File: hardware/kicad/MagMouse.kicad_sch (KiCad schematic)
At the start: 0 parts

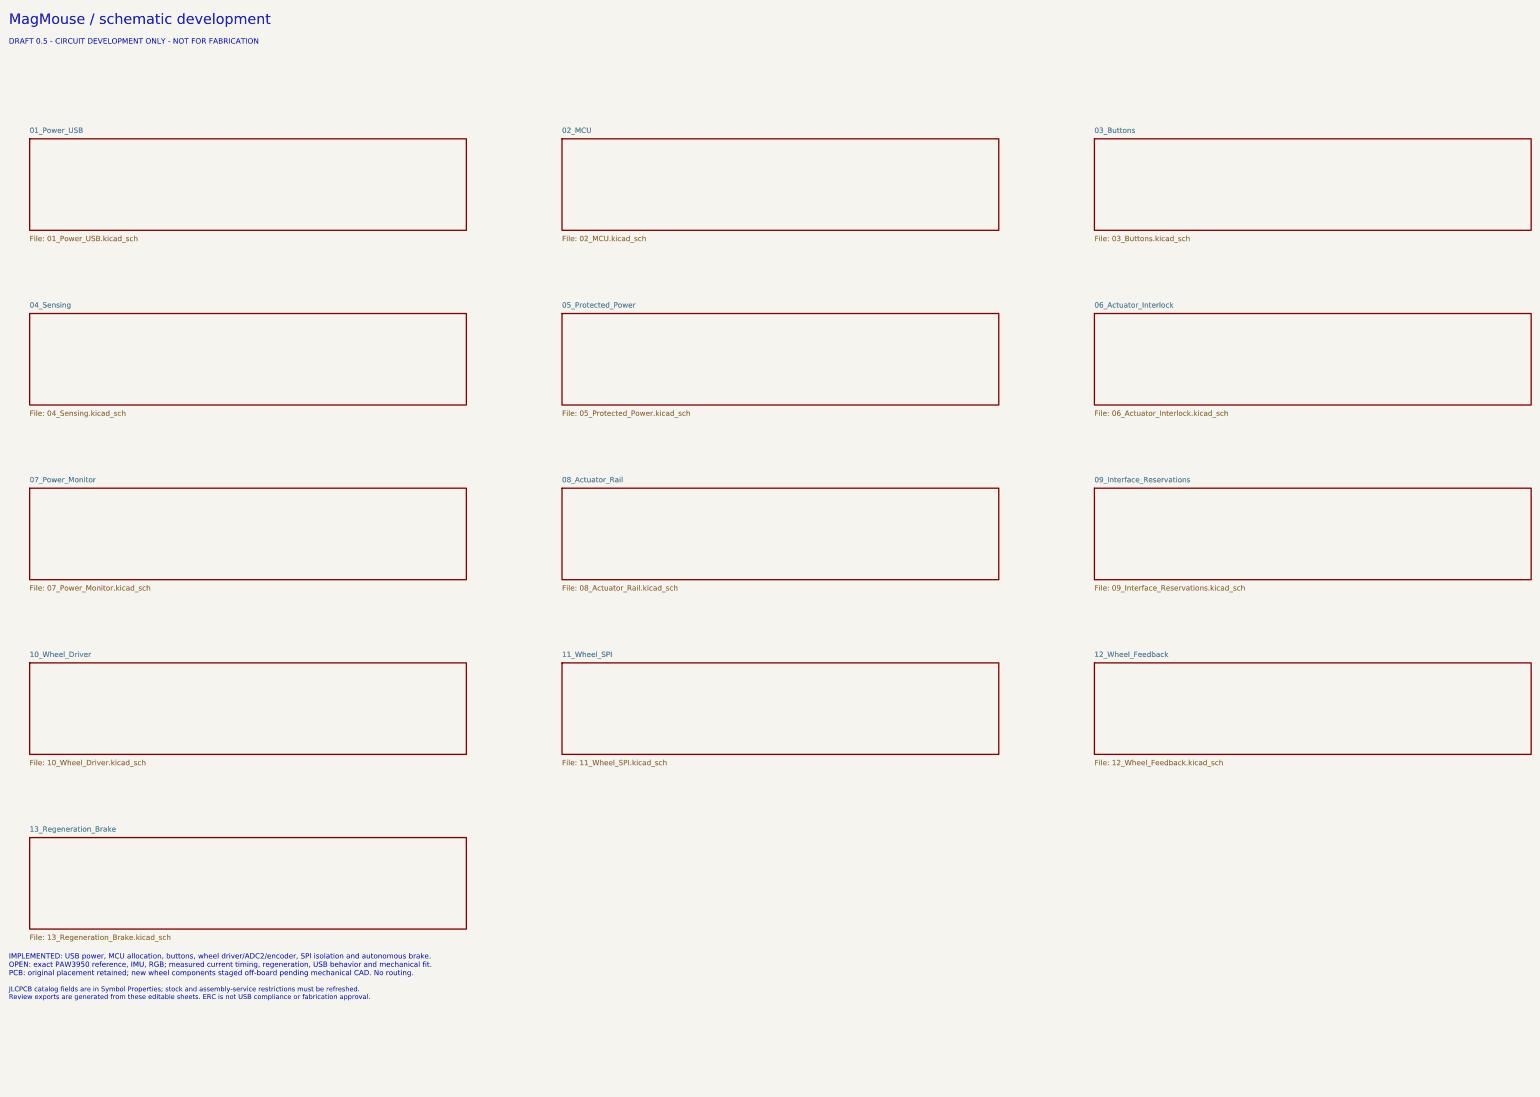
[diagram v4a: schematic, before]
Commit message: Add IMU and RGB circuits and document optical sourcing
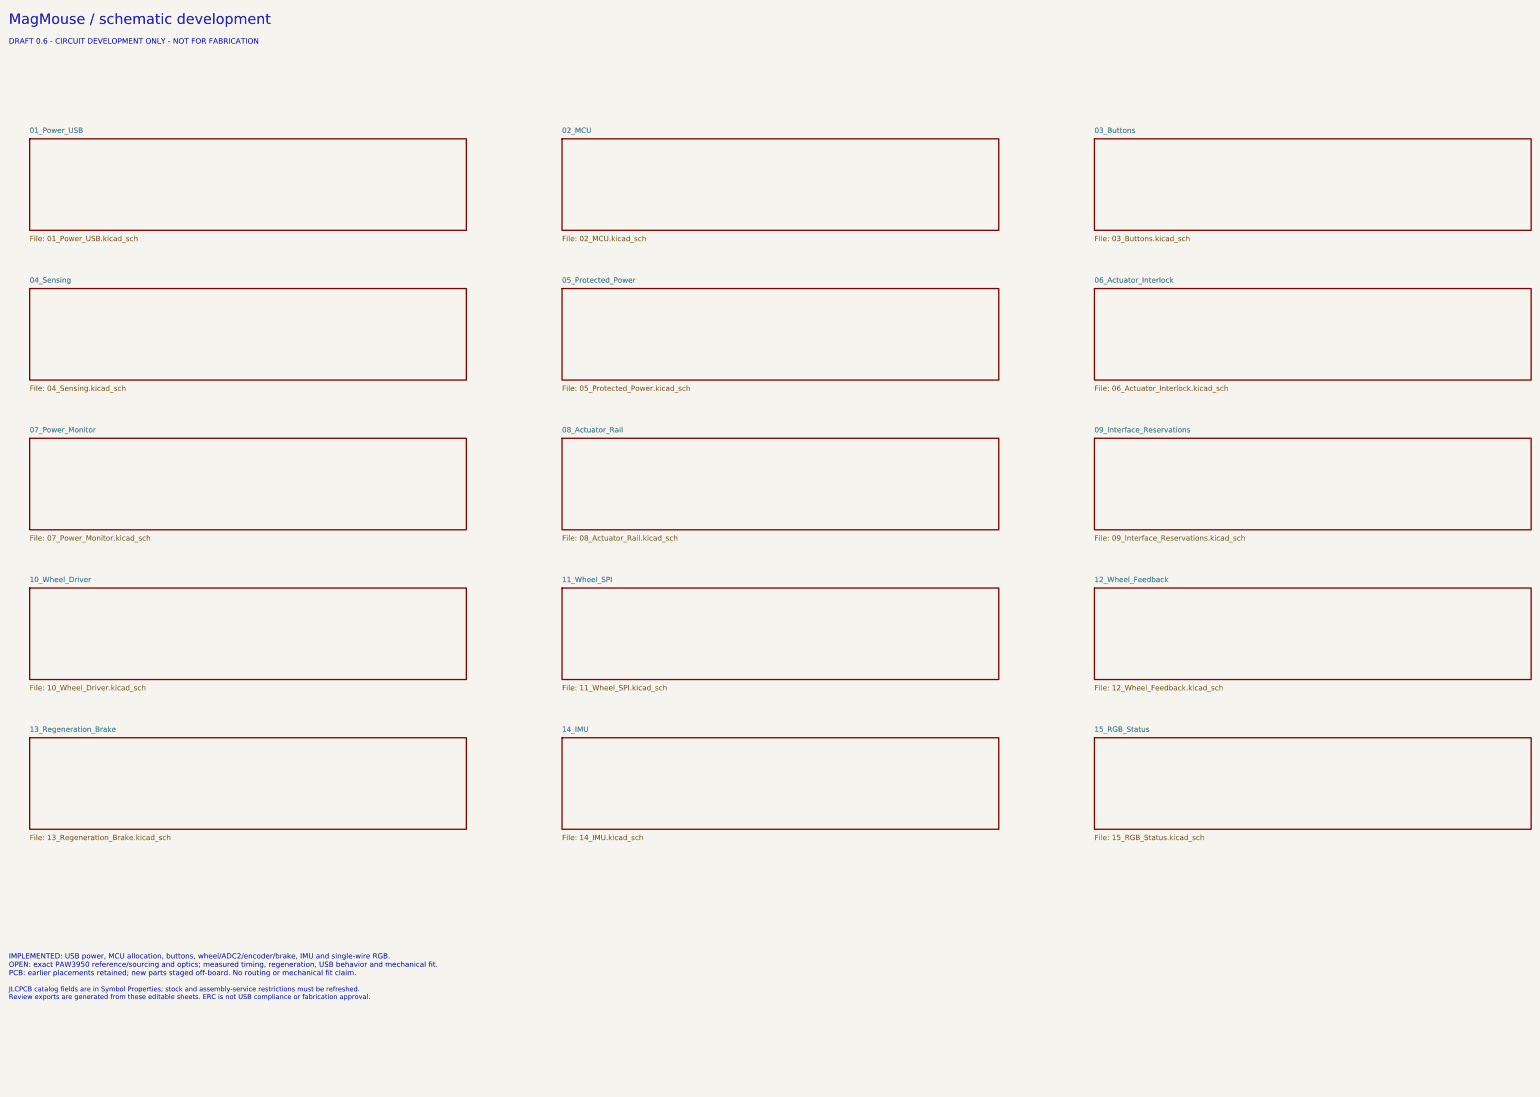
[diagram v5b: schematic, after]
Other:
- added sheet 14_IMU (14_IMU.kicad_sch)
- added sheet 15_RGB_Status (15_RGB_Status.kicad_sch)
- note added: "DRAFT 0.6 - CIRCUIT DEVELOPMENT ONLY - NOT FOR FABRICATION"
- note added: "IMPLEMENTED: USB power, MCU allocation, buttons, wheel/ADC2/encoder/brake, IMU and single-wire RGB. OPEN: exact PAW3950 reference/sourcing and optics; measured timing, regeneration, USB behavior and mechanical fit. PCB: earlier placements retained; new parts staged off-board. No routing or mechanical fit claim."
- note removed: "DRAFT 0.5 - CIRCUIT DEVELOPMENT ONLY - NOT FOR FABRICATION"
- note removed: "IMPLEMENTED: USB power, MCU allocation, buttons, wheel driver/ADC2/encoder, SPI isolation and autonomous brake. OPEN: exact PAW3950 reference, IMU, RGB; measured current timing, regeneration, USB behavior and mechanical fit. PCB: original placement retained; new wheel components staged off-board pending mechanical CAD. No routing."
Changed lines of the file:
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@@
     (title "MagMouse - MagMouse")
     (date "2026-09-09")
-    (rev "0.5 DRAFT")
+    (rev "0.6 DRAFT")
     (company "MagMouse")
     (comment 1 "NOT FOR FABRICATION - unresolved circuits listed in README.md"))
@@
       (justify left top))
 )
-  (text "DRAFT 0.5 - CIRCUIT DEVELOPMENT ONLY - NOT FOR FABRICATION"
+  (text "DRAFT 0.6 - CIRCUIT DEVELOPMENT ONLY - NOT FOR FABRICATION"
     (at 20 24 0)
     (effects
@@
           (page "4")))))
   (sheet
-    (at 25 90)
+    (at 25 84)
     (size 105 22)
     (stroke
@@
       (color 0 0 0 0))
     (property "Sheetname" "04_Sensing"
-      (at 25 88.73 0)
+      (at 25 82.73 0)
       (effects
         (font
@@
         (justify left bottom)))
     (property "Sheetfile" "04_Sensing.kicad_sch"
-      (at 25 113.27 0)
+      (at 25 107.27 0)
       (effects
         (font
@@
           (page "5")))))
   (sheet
-    (at 153 90)
+    (at 153 84)
     (size 105 22)
     (stroke
@@
       (color 0 0 0 0))
     (property "Sheetname" "05_Protected_Power"
-      (at 153 88.73 0)
+      (at 153 82.73 0)
       (effects
         (font
@@
         (justify left bottom)))
     (property "Sheetfile" "05_Protected_Power.kicad_sch"
-      (at 153 113.27 0)
+      (at 153 107.27 0)
       (effects
         (font
@@
           (page "6")))))
   (sheet
-    (at 281 90)
+    (at 281 84)
     (size 105 22)
     (stroke
@@
       (color 0 0 0 0))
     (property "Sheetname" "06_Actuator_Interlock"
-      (at 281 88.73 0)
+      (at 281 82.73 0)
       (effects
         (font
@@
         (justify left bottom)))
     (property "Sheetfile" "06_Actuator_Interlock.kicad_sch"
-      (at 281 113.27 0)
+      (at 281 107.27 0)
       (effects
         (font
@@
           (page "7")))))
   (sheet
-    (at 25 132)
+    (at 25 120)
     (size 105 22)
     (stroke
@@
       (color 0 0 0 0))
     (property "Sheetname" "07_Power_Monitor"
-      (at 25 130.73 0)
+      (at 25 118.73 0)
       (effects
         (font
@@
         (justify left bottom)))
     (property "Sheetfile" "07_Power_Monitor.kicad_sch"
-      (at 25 155.27 0)
+      (at 25 143.27 0)
       (effects
         (font
@@
           (page "8")))))
   (sheet
-    (at 153 132)
+    (at 153 120)
     (size 105 22)
     (stroke
@@
       (color 0 0 0 0))
     (property "Sheetname" "08_Actuator_Rail"
-      (at 153 130.73 0)
+      (at 153 118.73 0)
       (effects
         (font
@@
         (justify left bottom)))
     (property "Sheetfile" "08_Actuator_Rail.kicad_sch"
-      (at 153 155.27 0)
+      (at 153 143.27 0)
       (effects
         (font
@@
         (path "/5d73110b-42e6-5c5c-9841-c82d60f67640"
           (page "9")))))
-  (text "IMPLEMENTED: USB power, MCU allocation, buttons, wheel driver/ADC2/encoder, SPI isolation and autonomous brake.\nOPEN: exact PAW3950 reference, IMU, RGB; measured current timing, regeneration, USB behavior and mechanical fit.\nPCB: original placement retained; new wheel components staged off-board pending mechanical CAD. No routing."
+  (text "IMPLEMENTED: USB power, MCU allocation, buttons, wheel/ADC2/encoder/brake, IMU and single-wire RGB.\nOPEN: exact PAW3950 reference/sourcing and optics; measured timing, regeneration, USB behavior and mechanical fit.\nPCB: earlier placements retained; new parts staged off-board. No routing or mechanical fit claim."
     (at 20 244 0)
     (effects
@@
   (embedded_fonts no)
   (sheet
-    (at 281 132)
+    (at 281 120)
     (size 105 22)
     (stroke
@@
       (color 0 0 0 0))
     (property "Sheetname" "09_Interface_Reservations"
-      (at 281 130.73 0)
+      (at 281 118.73 0)
       (effects
         (font
@@
         (justify left bottom)))
     (property "Sheetfile" "09_Interface_Reservations.kicad_sch"
-      (at 281 155.27 0)
+      (at 281 143.27 0)
       (effects
         (font
@@
           (page "10")))))
   (sheet
-    (at 25 174)
+    (at 25 156)
     (size 105 22)
     (stroke
@@
       (color 0 0 0 0))
     (property "Sheetname" "10_Wheel_Driver"
-      (at 25 172.73 0)
+      (at 25 154.73 0)
       (effects
         (font
@@
         (justify left bottom)))
     (property "Sheetfile" "10_Wheel_Driver.kicad_sch"
-      (at 25 197.27 0)
+      (at 25 179.27 0)
       (effects
         (font
@@
           (page "11")))))
   (sheet
-    (at 153 174)
+    (at 153 156)
     (size 105 22)
     (stroke
@@
       (color 0 0 0 0))
     (property "Sheetname" "11_Wheel_SPI"
-      (at 153 172.73 0)
+      (at 153 154.73 0)
       (effects
         (font
@@
         (justify left bottom)))
     (property "Sheetfile" "11_Wheel_SPI.kicad_sch"
-      (at 153 197.27 0)
+      (at 153 179.27 0)
       (effects
         (font
@@
           (page "12")))))
   (sheet
-    (at 281 174)
+    (at 281 156)
     (size 105 22)
     (stroke
@@
       (color 0 0 0 0))
     (property "Sheetname" "12_Wheel_Feedback"
-      (at 281 172.73 0)
+      (at 281 154.73 0)
       (effects
         (font
@@
         (justify left bottom)))
     (property "Sheetfile" "12_Wheel_Feedback.kicad_sch"
-      (at 281 197.27 0)
+      (at 281 179.27 0)
       (effects
         (font
@@
           (page "13")))))
   (sheet
-    (at 25 216)
+    (at 25 192)
     (size 105 22)
     (stroke
@@
       (color 0 0 0 0))
     (property "Sheetname" "13_Regeneration_Brake"
-      (at 25 214.73 0)
+      (at 25 190.73 0)
       (effects
         (font
@@
         (justify left bottom)))
     (property "Sheetfile" "13_Regeneration_Brake.kicad_sch"
-      (at 25 239.27 0)
-      (effects
-        (font
-          (size 1.27 1.27))
-        (justify left top)))
-    (instances
-      (project "MagMouse"
-        (path "/5d73110b-42e6-5c5c-9841-c82d60f67640"
-          (page "14"))))))
+      (at 25 215.27 0)
+      (effects
+        (font
+          (size 1.27 1.27))
+        (justify left top)))
+    (instances
+      (project "MagMouse"
+        (path "/5d73110b-42e6-5c5c-9841-c82d60f67640"
+          (page "14")))))
+  (sheet
+    (at 153 192)
+    (size 105 22)
+    (stroke
+      (width 0.254)
+      (type default))
+    (fill
+      (color 0 0 0 0))
+    (property "Sheetname" "14_IMU"
+      (at 153 190.73 0)
+      (effects
+        (font
+          (size 1.27 1.27))
+        (justify left bottom)))
+    (property "Sheetfile" "14_IMU.kicad_sch"
+      (at 153 215.27 0)
+      (effects
+        (font
+          (size 1.27 1.27))
+        (justify left top)))
+    (instances
+      (project "MagMouse"
+        (path "/5d73110b-42e6-5c5c-9841-c82d60f67640"
+          (page "15")))))
+  (sheet
+    (at 281 192)
+    (size 105 22)
+    (stroke
+      (width 0.254)
+      (type default))
+    (fill
+      (color 0 0 0 0))
+    (property "Sheetname" "15_RGB_Status"
+      (at 281 190.73 0)
+      (effects
+        (font
+          (size 1.27 1.27))
+        (justify left bottom)))
+    (property "Sheetfile" "15_RGB_Status.kicad_sch"
+      (at 281 215.27 0)
+      (effects
+        (font
+          (size 1.27 1.27))
+        (justify left top)))
+    (instances
+      (project "MagMouse"
+        (path "/5d73110b-42e6-5c5c-9841-c82d60f67640"
+          (page "16"))))))

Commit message: Add PMW3360 optical circuitry and PCB-first mechanical datum
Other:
- added sheet 16_Optical_Power (16_Optical_Power.kicad_sch)
- added sheet 17_Optical_Sensor (17_Optical_Sensor.kicad_sch)
- note added: "DRAFT 0.7 - CIRCUIT DEVELOPMENT ONLY - NOT FOR FABRICATION"
- note added: "IMPLEMENTED: power, MCU, buttons, wheel/brake, IMU, RGB and PMW3360 optical circuit. OPEN: samples/SROM rights, optical fit, measured timing, USB behavior, power/thermal and mechanical acceptance."
- note added: "JLCPCB catalog IDs are not stock or assembly approval. PCB is unrouted; optical parts are staged."
- note removed: "DRAFT 0.6 - CIRCUIT DEVELOPMENT ONLY - NOT FOR FABRICATION"
- note removed: "IMPLEMENTED: USB power, MCU allocation, buttons, wheel/ADC2/encoder/brake, IMU and single-wire RGB. OPEN: exact PAW3950 reference/sourcing and optics; measured timing, regeneration, USB behavior and mechanical fit. PCB: earlier placements retained; new parts staged off-board. No routing or mechanical fit claim."
- note removed: "JLCPCB catalog fields are in Symbol Properties; stock and assembly-service restrictions must be refreshed. Review exports are generated from these editable sheets. ERC is not USB compliance or fabrication approval."
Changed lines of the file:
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@@
     (title "MagMouse - MagMouse")
     (date "2026-09-09")
-    (rev "0.6 DRAFT")
+    (rev "0.7 DRAFT")
     (company "MagMouse")
     (comment 1 "NOT FOR FABRICATION - unresolved circuits listed in README.md"))
@@
       (justify left top))
 )
-  (text "DRAFT 0.6 - CIRCUIT DEVELOPMENT ONLY - NOT FOR FABRICATION"
+  (text "DRAFT 0.7 - CIRCUIT DEVELOPMENT ONLY - NOT FOR FABRICATION"
     (at 20 24 0)
     (effects
@@
         (path "/5d73110b-42e6-5c5c-9841-c82d60f67640"
           (page "9")))))
-  (text "IMPLEMENTED: USB power, MCU allocation, buttons, wheel/ADC2/encoder/brake, IMU and single-wire RGB.\nOPEN: exact PAW3950 reference/sourcing and optics; measured timing, regeneration, USB behavior and mechanical fit.\nPCB: earlier placements retained; new parts staged off-board. No routing or mechanical fit claim."
-    (at 20 244 0)
+  (text "IMPLEMENTED: power, MCU, buttons, wheel/brake, IMU, RGB and PMW3360 optical circuit.\nOPEN: samples/SROM rights, optical fit, measured timing, USB behavior, power/thermal and mechanical acceptance."
+    (at 20 260 0)
     (effects
       (font
-        (size 1.25 1.25))
+        (size 1.1 1.1))
       (justify left top))
 )
-  (text "JLCPCB catalog fields are in Symbol Properties; stock and assembly-service restrictions must be refreshed.\nReview exports are generated from these editable sheets. ERC is not USB compliance or fabrication approval."
-    (at 20 252 0)
+  (text "JLCPCB catalog IDs are not stock or assembly approval. PCB is unrouted; optical parts are staged."
+    (at 20 273 0)
     (effects
       (font
-        (size 1.15 1.15))
+        (size 1.1 1.1))
       (justify left top))
 )
@@
       (project "MagMouse"
         (path "/5d73110b-42e6-5c5c-9841-c82d60f67640"
-          (page "16"))))))
+          (page "16")))))
+  (sheet
+    (at 25 228)
+    (size 105 22)
+    (stroke
+      (width 0.254)
+      (type default))
+    (fill
+      (color 0 0 0 0))
+    (property "Sheetname" "16_Optical_Power"
+      (at 25 226.73 0)
+      (effects
+        (font
+          (size 1.27 1.27))
+        (justify left bottom)))
+    (property "Sheetfile" "16_Optical_Power.kicad_sch"
+      (at 25 251.27 0)
+      (effects
+        (font
+          (size 1.27 1.27))
+        (justify left top)))
+    (instances
+      (project "MagMouse"
+        (path "/5d73110b-42e6-5c5c-9841-c82d60f67640"
+          (page "17")))))
+  (sheet
+    (at 153 228)
+    (size 105 22)
+    (stroke
+      (width 0.254)
+      (type default))
+    (fill
+      (color 0 0 0 0))
+    (property "Sheetname" "17_Optical_Sensor"
+      (at 153 226.73 0)
+      (effects
+        (font
+          (size 1.27 1.27))
+        (justify left bottom)))
+    (property "Sheetfile" "17_Optical_Sensor.kicad_sch"
+      (at 153 251.27 0)
+      (effects
+        (font
+          (size 1.27 1.27))
+        (justify left top)))
+    (instances
+      (project "MagMouse"
+        (path "/5d73110b-42e6-5c5c-9841-c82d60f67640"
+          (page "18"))))))

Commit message: Place motherboard, add upright encoder PCB and route logic buck
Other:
- note added: "DRAFT 0.8 - CIRCUIT DEVELOPMENT ONLY - NOT FOR FABRICATION"
- note added: "JLCPCB catalog IDs are not stock or assembly approval. Motherboard buck is routed; full-board routing remains open. Optics are placed. U27/C62 are on the separate routed 14 x 18 mm Encoder board; cable and mechanical fit remain unverified."
- note removed: "DRAFT 0.7 - CIRCUIT DEVELOPMENT ONLY - NOT FOR FABRICATION"
- note removed: "JLCPCB catalog IDs are not stock or assembly approval. PCB is unrouted; optical parts are staged."
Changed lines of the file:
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@@
     (title "MagMouse - MagMouse")
     (date "2026-09-09")
-    (rev "0.7 DRAFT")
+    (rev "0.8 DRAFT")
     (company "MagMouse")
     (comment 1 "NOT FOR FABRICATION - unresolved circuits listed in README.md"))
@@
       (justify left top))
 )
-  (text "DRAFT 0.7 - CIRCUIT DEVELOPMENT ONLY - NOT FOR FABRICATION"
+  (text "DRAFT 0.8 - CIRCUIT DEVELOPMENT ONLY - NOT FOR FABRICATION"
     (at 20 24 0)
     (effects
@@
       (justify left top))
 )
-  (text "JLCPCB catalog IDs are not stock or assembly approval. PCB is unrouted; optical parts are staged."
+  (text "JLCPCB catalog IDs are not stock or assembly approval. Motherboard buck is routed; full-board routing remains open. Optics are placed.\nU27/C62 are on the separate routed 14 x 18 mm Encoder board; cable and mechanical fit remain unverified."
     (at 20 273 0)
     (effects
